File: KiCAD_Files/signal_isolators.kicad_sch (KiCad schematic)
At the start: 9 parts, among them U801 ISO7720DWV, U802 ISO7720DWV, U803 ISO7330C

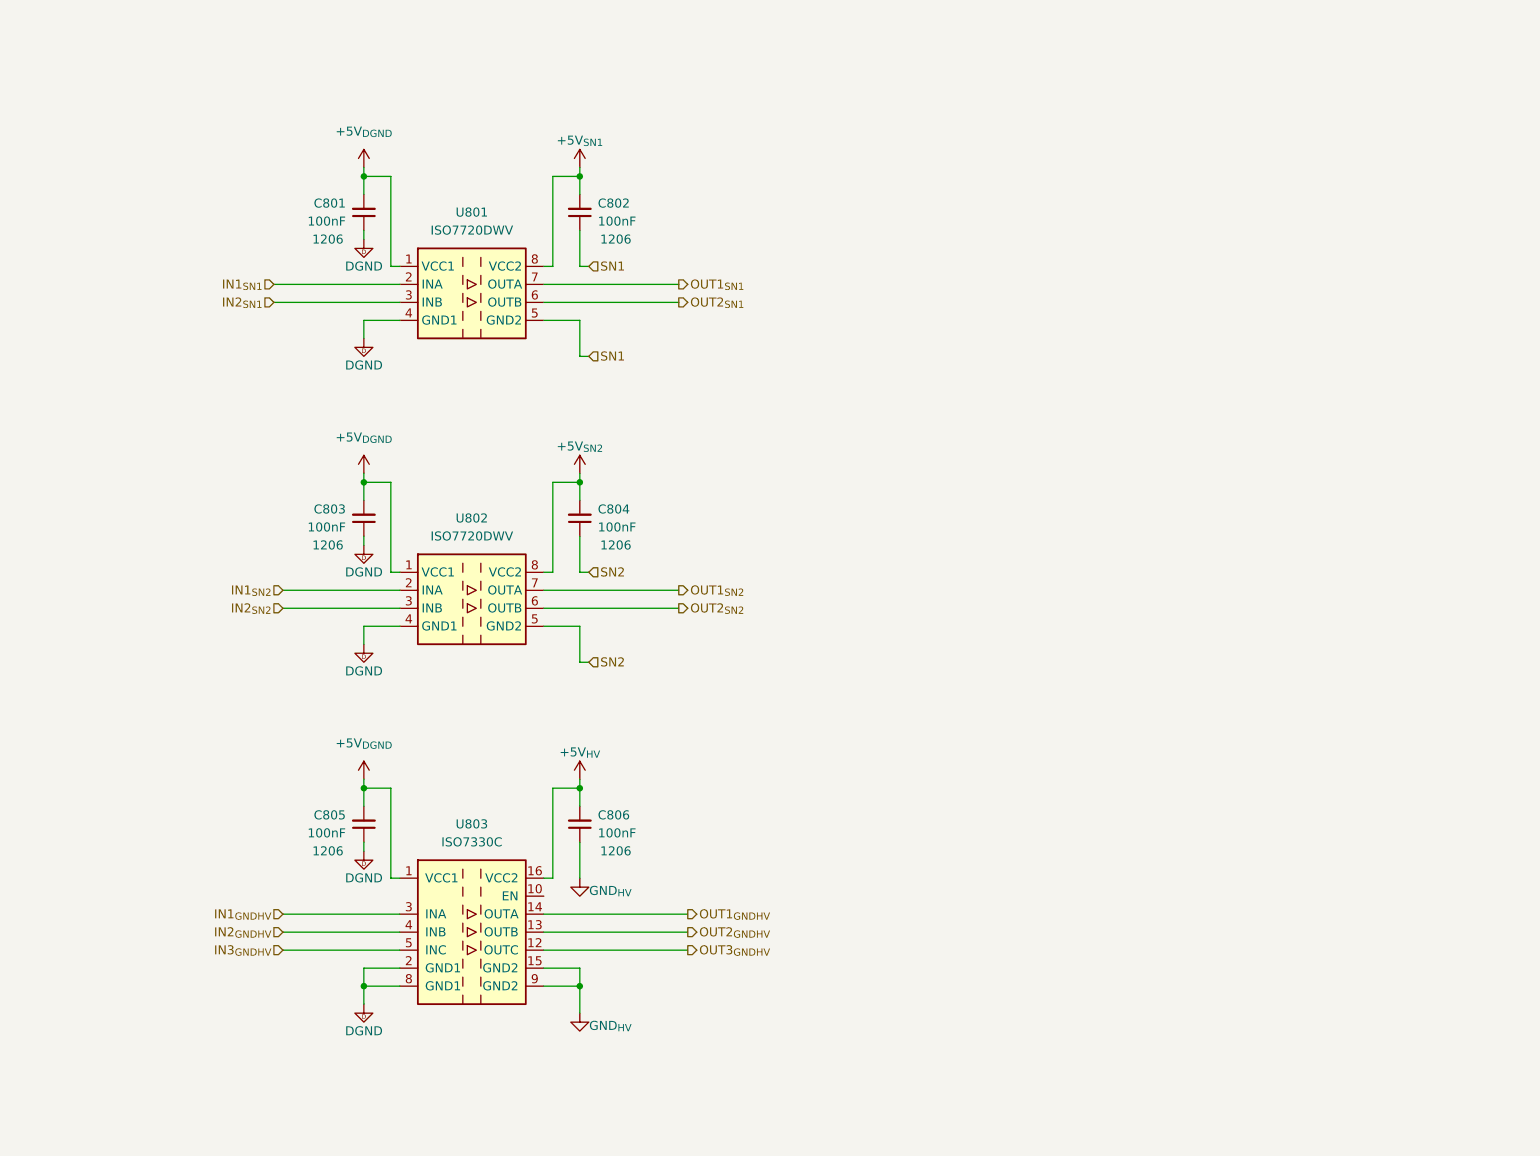
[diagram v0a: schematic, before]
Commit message: First routing pass complete.
Signed-off-by: Jean Alinei <jean.alinei@owntech.org>
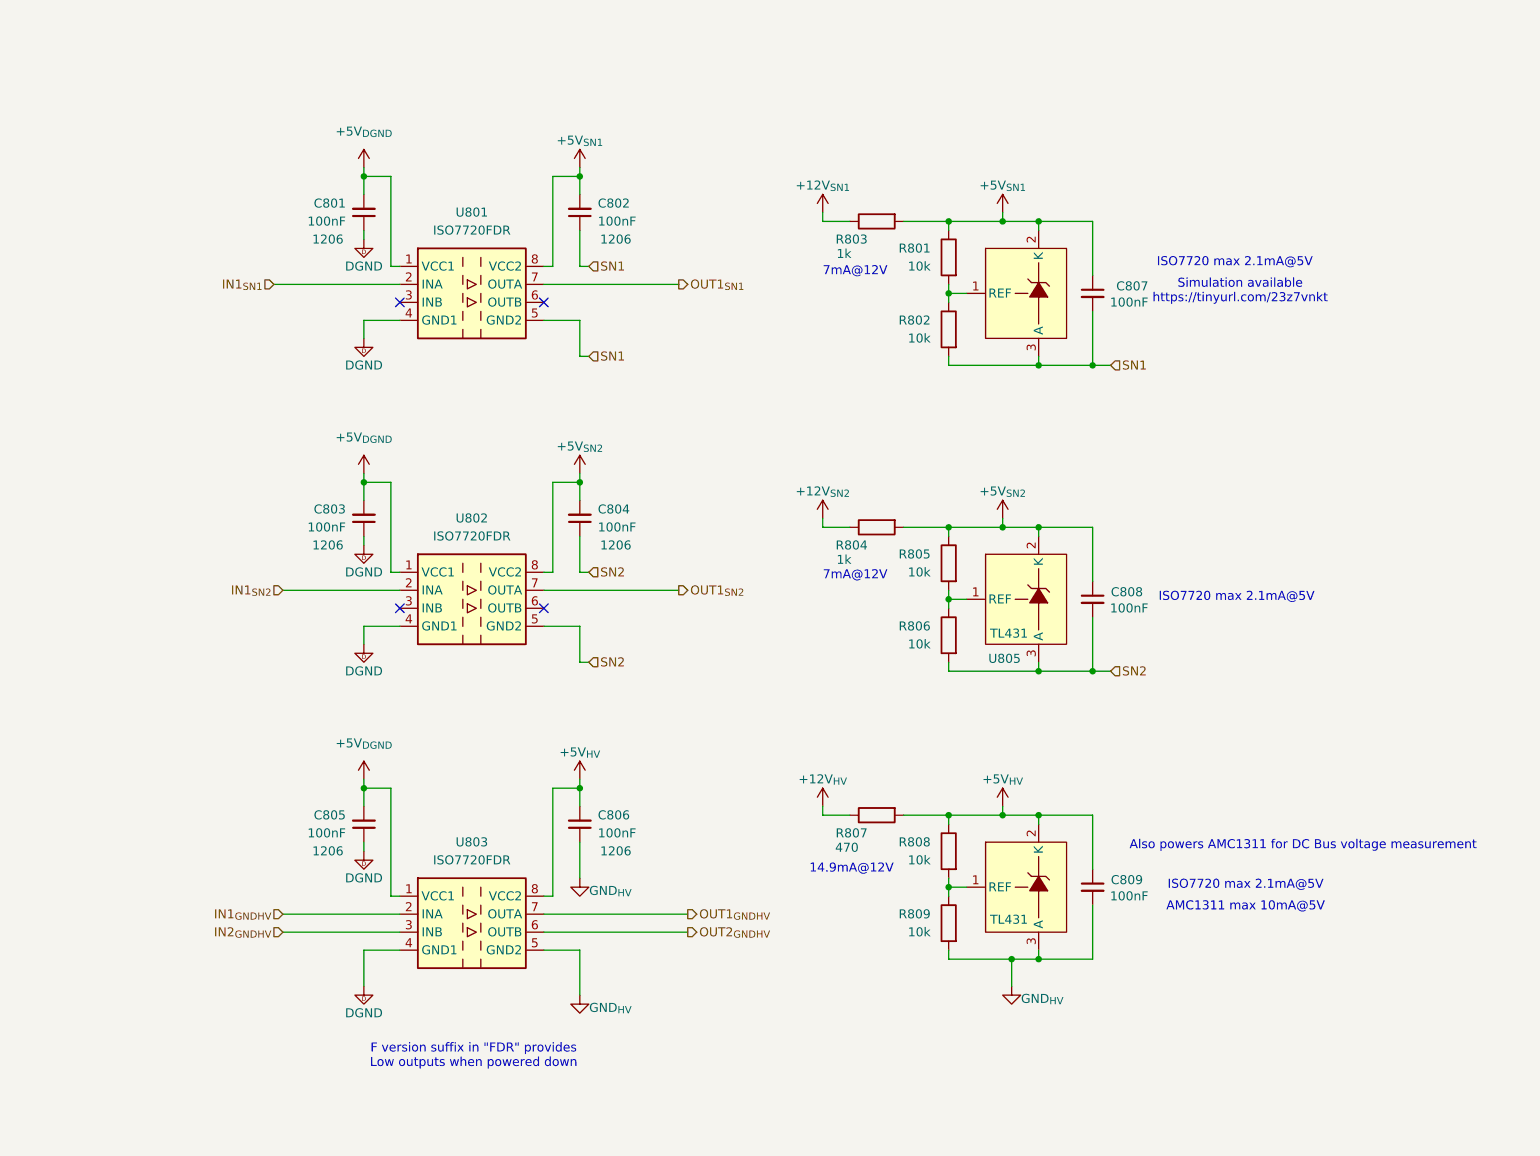
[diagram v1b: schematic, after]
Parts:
- added C807, C808, C809: 100nF, Capacitor_SMD:C_0805_2012Metric, symbol Device:C_Small
- added R801, R802, R805, R806, R808, R809: 10k, Capacitor_SMD:C_0805_2012Metric, symbol Device:R
- added R803, R804: 1k, Capacitor_SMD:C_0805_2012Metric, symbol Device:R
- added R807: 470, Capacitor_SMD:C_0805_2012Metric, symbol Device:R
- added U804: TL431DBZ, Package_TO_SOT_SMD:SOT-23, symbol Symbols:TL431
- added U805, U806: TL431, Package_TO_SOT_SMD:SOT-23, symbol Symbols:TL431
- U801, U802: value ISO7720DWV -> ISO7720FDR; footprint Package_SO:SOIC-8_7.5x5.85mm_P1.27mm -> Package_SO:SOIC-8_3.9x4.9mm_P1.27mm; LCSC (none) -> C2878308
- U803: value ISO7330C -> ISO7720FDR; footprint Package_SO:SOIC-16W_7.5x10.3mm_P1.27mm -> Package_SO:SOIC-8_3.9x4.9mm_P1.27mm; symbol Isolator:ISO7330C -> Isolator:ISO7720DWV; LCSC (none) -> C2878308
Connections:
- net IN3_{GNDHV} is gone; now on net GND_{HV}: U803.5 (GND2)
- net +5V_{HV}: now also U803.8 (VCC2), C809.1, R807.2, R808.1, U806.2 (K); no longer U803.16 (VCC2)
- net +5V_{SN1}: now also C807.1, R801.1, R803.2, U804.2 (K)
- net +5V_{SN2}: now also C808.1, R804.2, R805.1, U805.2 (K)
- net DGND: now also U803.4 (GND1); no longer U803.2 (GND1), U803.8 (GND1)
- net GND_{HV}: now also C809.2, R809.2, U806.3 (A); no longer U803.15 (GND2), U803.9 (GND2)
- net IN1_{GNDHV}: now also U803.2 (INA); no longer U803.3 (INA)
- net IN2_{GNDHV}: now also U803.3 (INB); no longer U803.4 (INB)
- net OUT1_{GNDHV}: now also U803.7 (OUTA); no longer U803.14 (OUTA)
- net OUT2_{GNDHV}: now also U803.6 (OUTB); no longer U803.13 (OUTB)
- net SN1: now also C807.2, R802.2, U804.3 (A)
- net SN2: now also C808.2, R806.2, U805.3 (A)
- net IN2_{SN1}: no longer names the net of U801.3 (INB)
- net IN2_{SN2}: no longer names the net of U802.3 (INB)
- net OUT2_{SN1}: no longer names the net of U801.6 (OUTB)
- net OUT2_{SN2}: no longer names the net of U802.6 (OUTB)
- removed net OUT3_{GNDHV}: U803.12 (OUTC)
- new net: R801.2, R802.1, U804.1 (REF)
- new net: R808.2, R809.1, U806.1 (REF)
- new net: R805.2, R806.1, U805.1 (REF)
- new net +12V_{HV}: R807.1
- new net +12V_{SN1}: R803.1
- new net +12V_{SN2}: R804.1
- no-connect marks 0 -> 4
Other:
- note added: "14.9mA@12V"
- note added: "7mA@12V"
- note added: "AMC1311 max 10mA@5V"
- note added: "Also powers AMC1311 for DC Bus voltage measurement"
- note added: "F version suffix in "FDR" provides Low outputs when powered down"
- note added: "ISO7720 max 2.1mA@5V"
- note added: "Simulation available https://tinyurl.com/23z7vnkt"

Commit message: Added DRC rules according to IEC60664 and IPC2221.
Signed-off-by: Jean Alinei <jean.alinei@owntech.org>
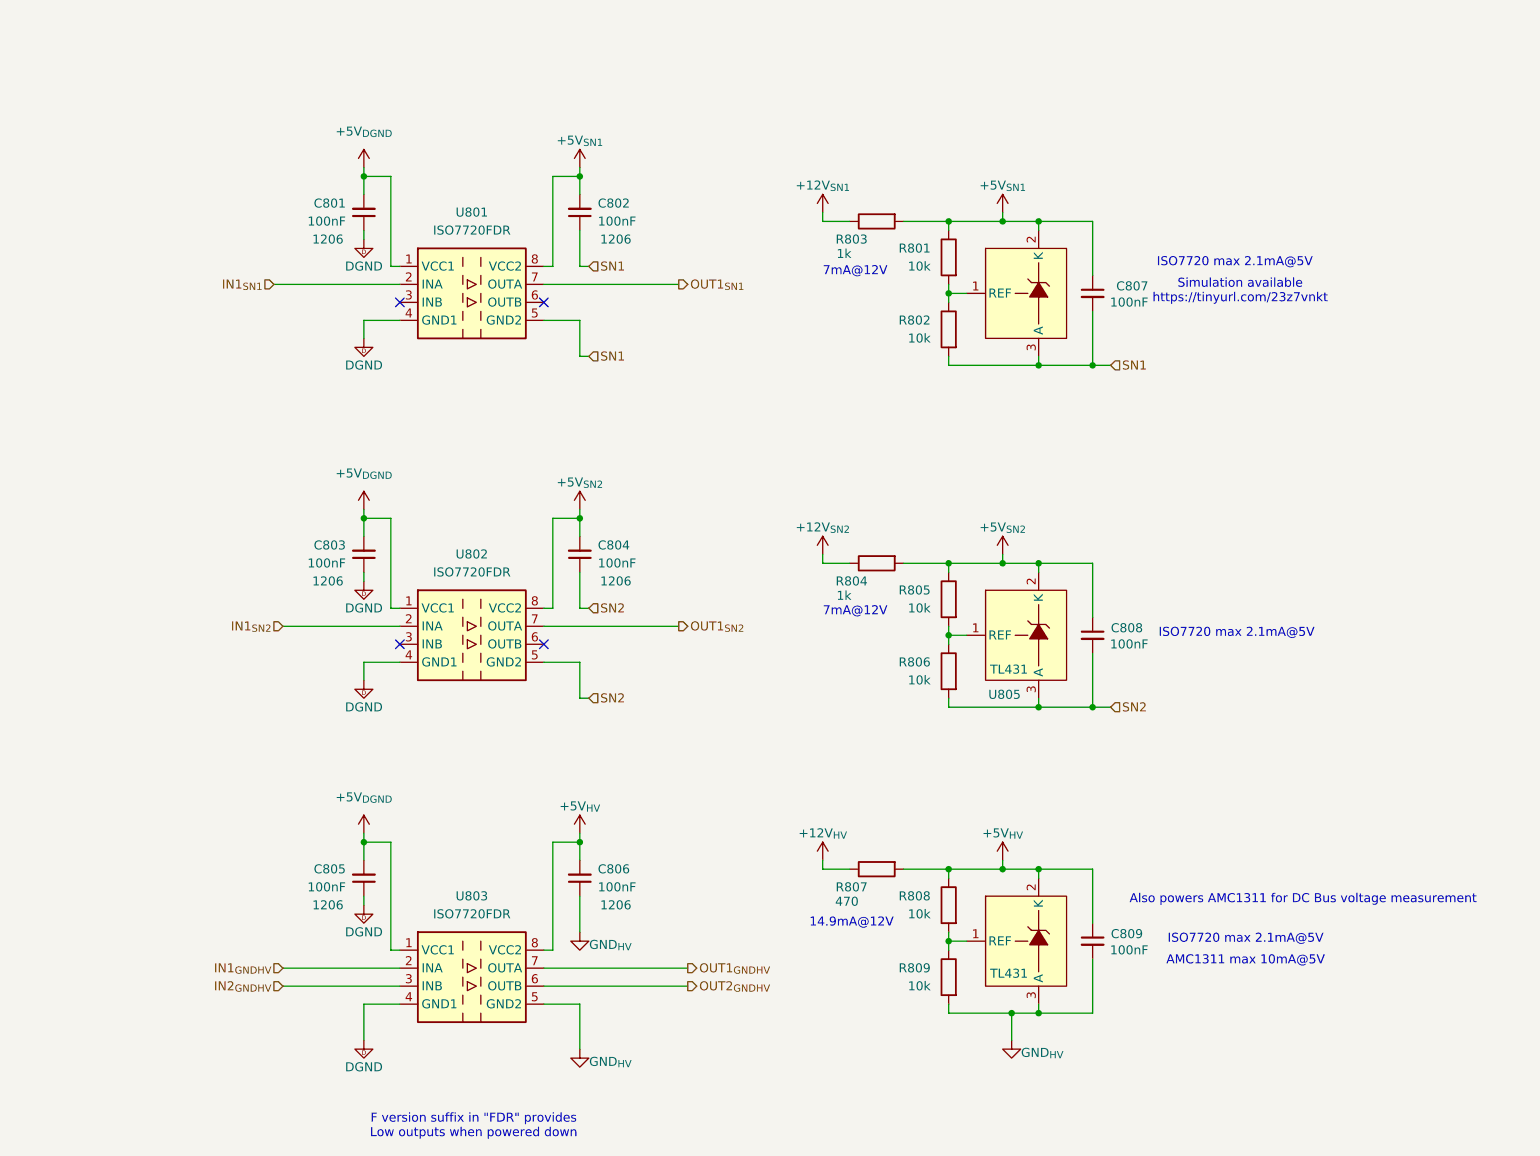
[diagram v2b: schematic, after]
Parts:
- C804: footprint Capacitor_SMD:C_1206_3216Metric -> Capacitor_SMD:C_0805_2012Metric
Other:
- moved on the sheet: C803, C804, C805, C806, C808, C809, R804, R805, R806, R807, R808, R809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

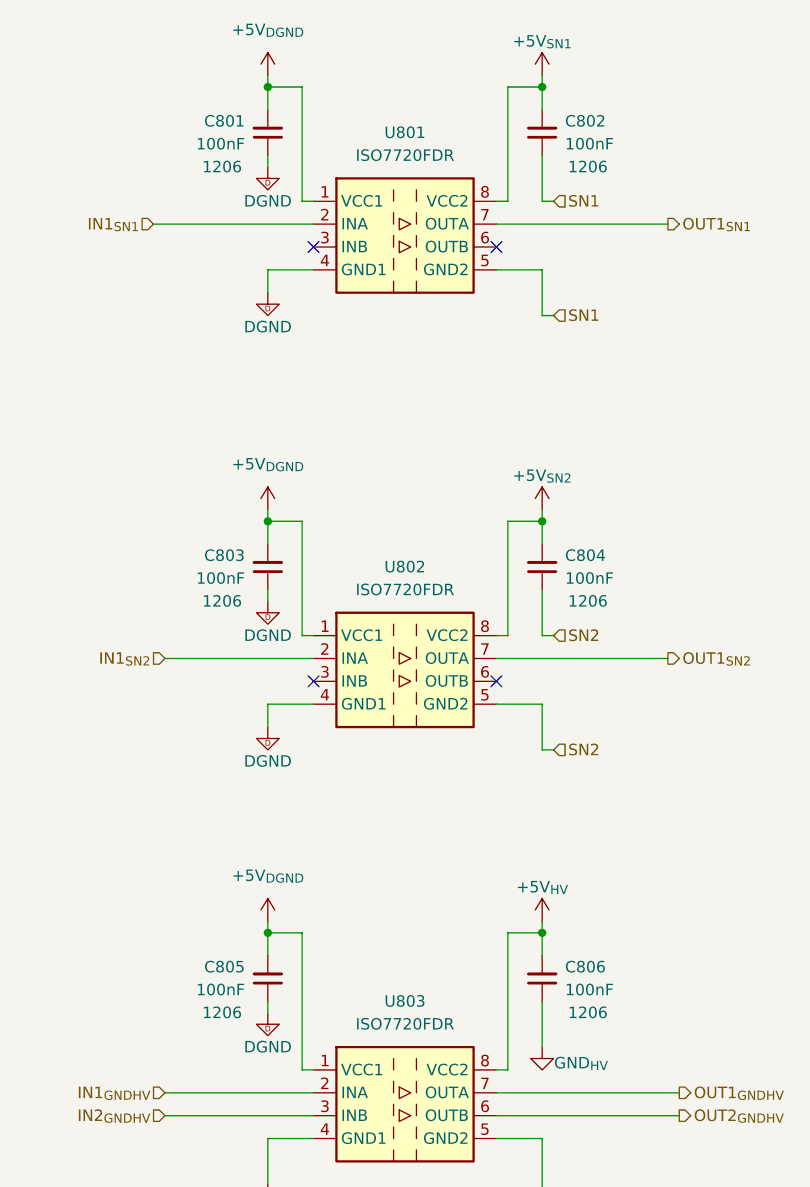
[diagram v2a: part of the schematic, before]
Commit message: Added passive references. Added ESD protection for MCU pins.
Signed-off-by: Jean Alinei <jean.alinei@owntech.org>
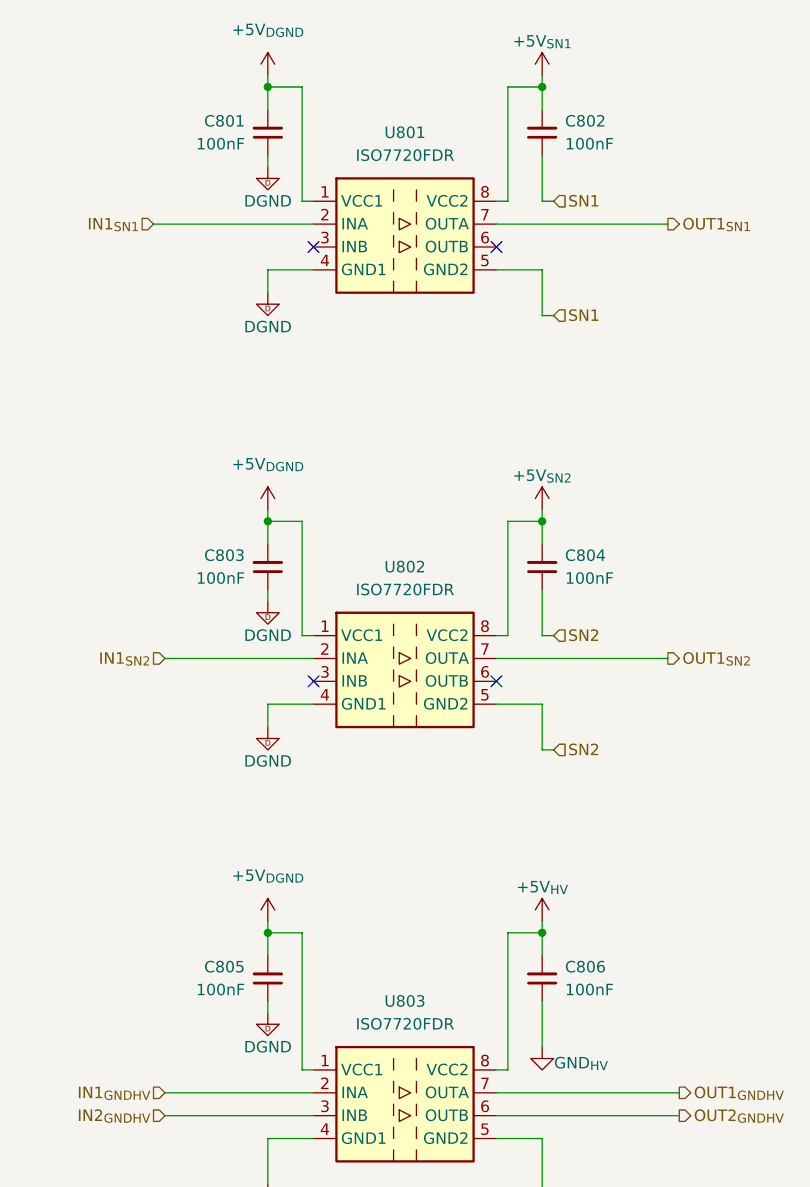
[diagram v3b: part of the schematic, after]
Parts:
- C801, C802, C803, C805, C806: Dielectric X7R -> (none); Functional Block Measurement -> (none); LCSC C5449000 -> C24497; Metal content BaTiO3 -> (none); Package 1206 -> (none); Subfunction VIHigh measure -> (none); Voltage 50V -> (none); manf# C1206C104K5RAC7867 -> (none)
- C804: Dielectric X7R -> (none); Functional Block Measurement -> (none); LCSC C5449000 -> C49678; Metal content BaTiO3 -> (none); Package 1206 -> (none); Subfunction VIHigh measure -> (none); Voltage 50V -> (none); manf# C1206C104K5RAC7867 -> (none)
- C807, C808, C809: Dielectric X7R -> (none); LCSC C5449000 -> C49678; Package 1206 -> (none); Voltage 50V -> (none); manf# C1206C104K5RAC7867 -> (none)
- R801, R802, R805, R806, R808, R809: LCSC (none) -> C17414
- R803, R804: LCSC (none) -> C17513
- R807: LCSC (none) -> C17710
- U804: value TL431DBZ -> TL431; LCSC (none) -> C181103
- U805, U806: LCSC (none) -> C181103
